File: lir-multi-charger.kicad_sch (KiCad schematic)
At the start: 46 parts, among them J1 USB_C_Receptacle_USB2.0_16P, J2 Conn_01x02_Pin, J3 Conn_01x02_Pin, J4 Conn_01x02_Pin, J5 Conn_01x02_Pin, J6 Conn_01x02_Pin, J7 Conn_01x02_Socket, J8 Conn_01x02_Socket, J9 Conn_01x02_Socket, U1 CN3130, U2 CN3130, U3 CN3130

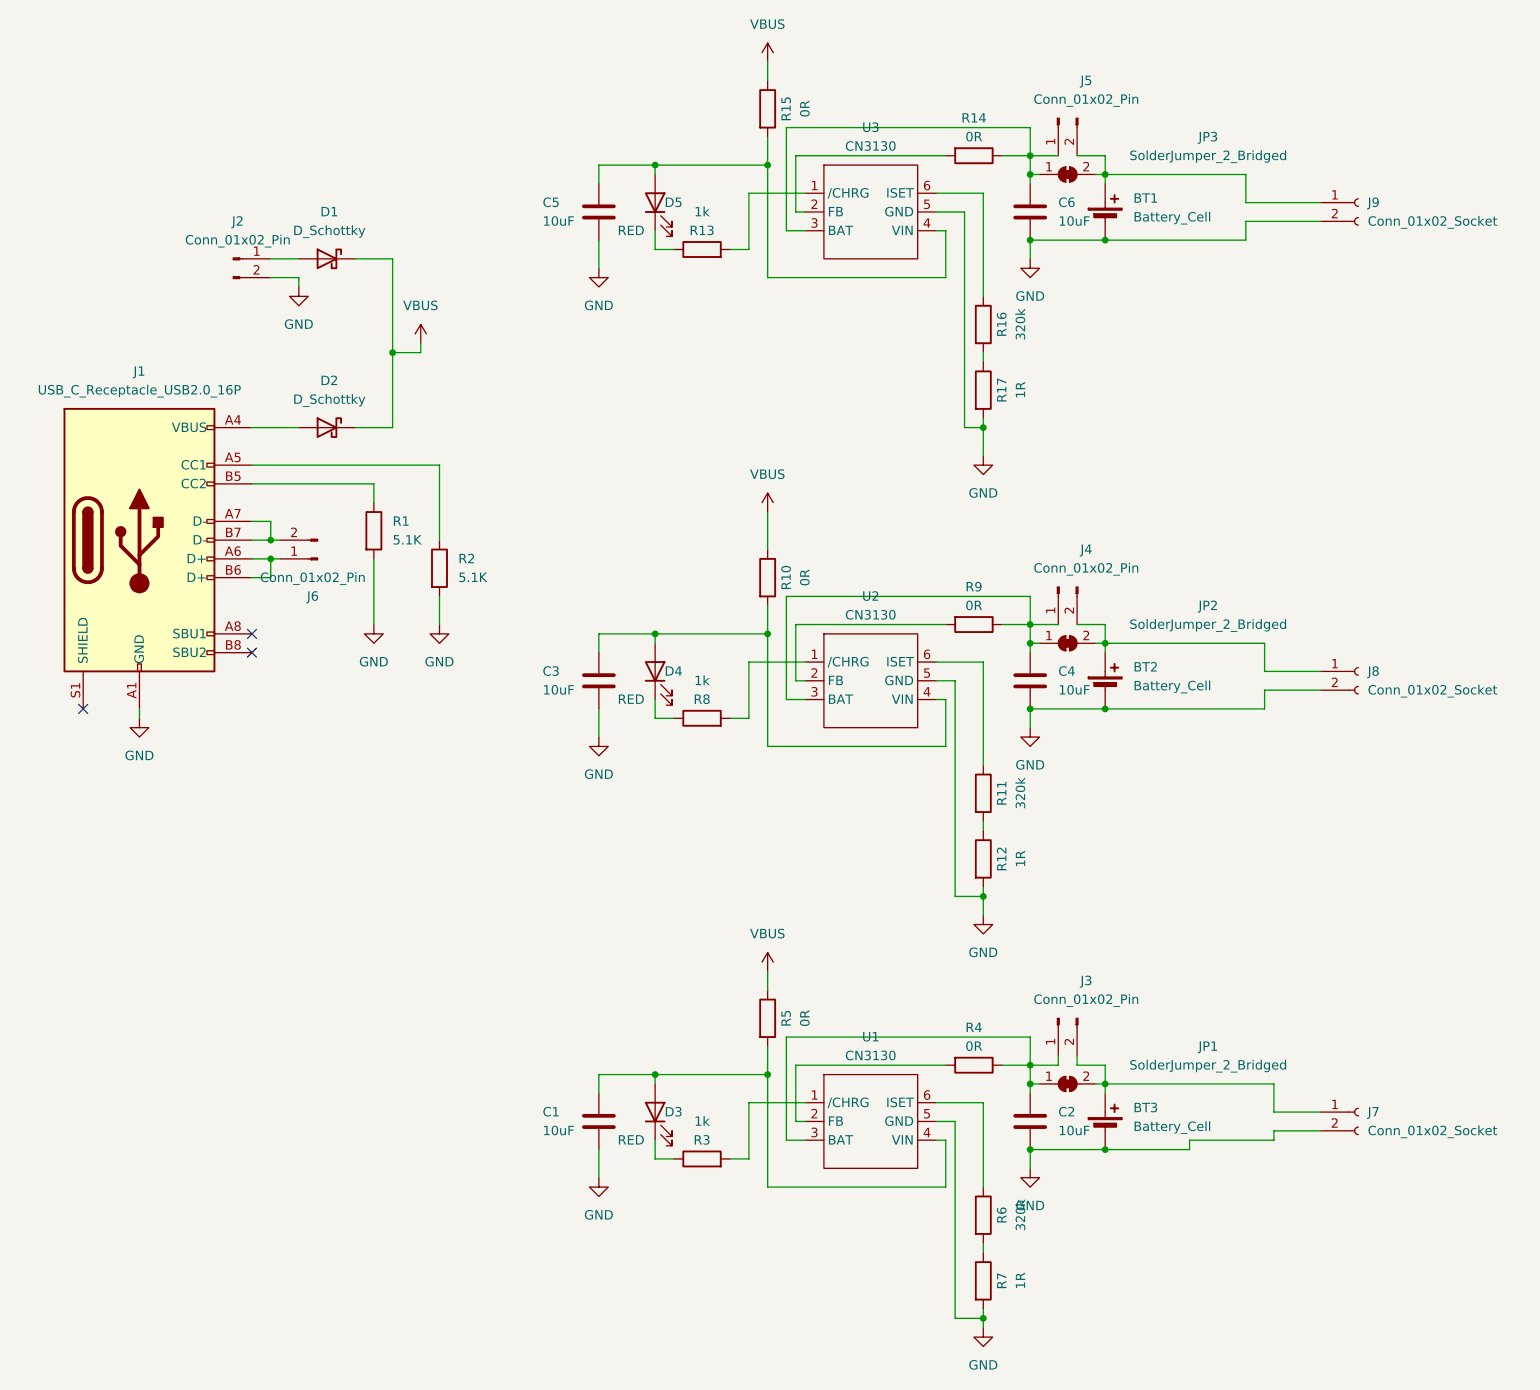
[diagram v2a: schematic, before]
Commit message: Update PCB design: modify resistor values and add labels for better readability
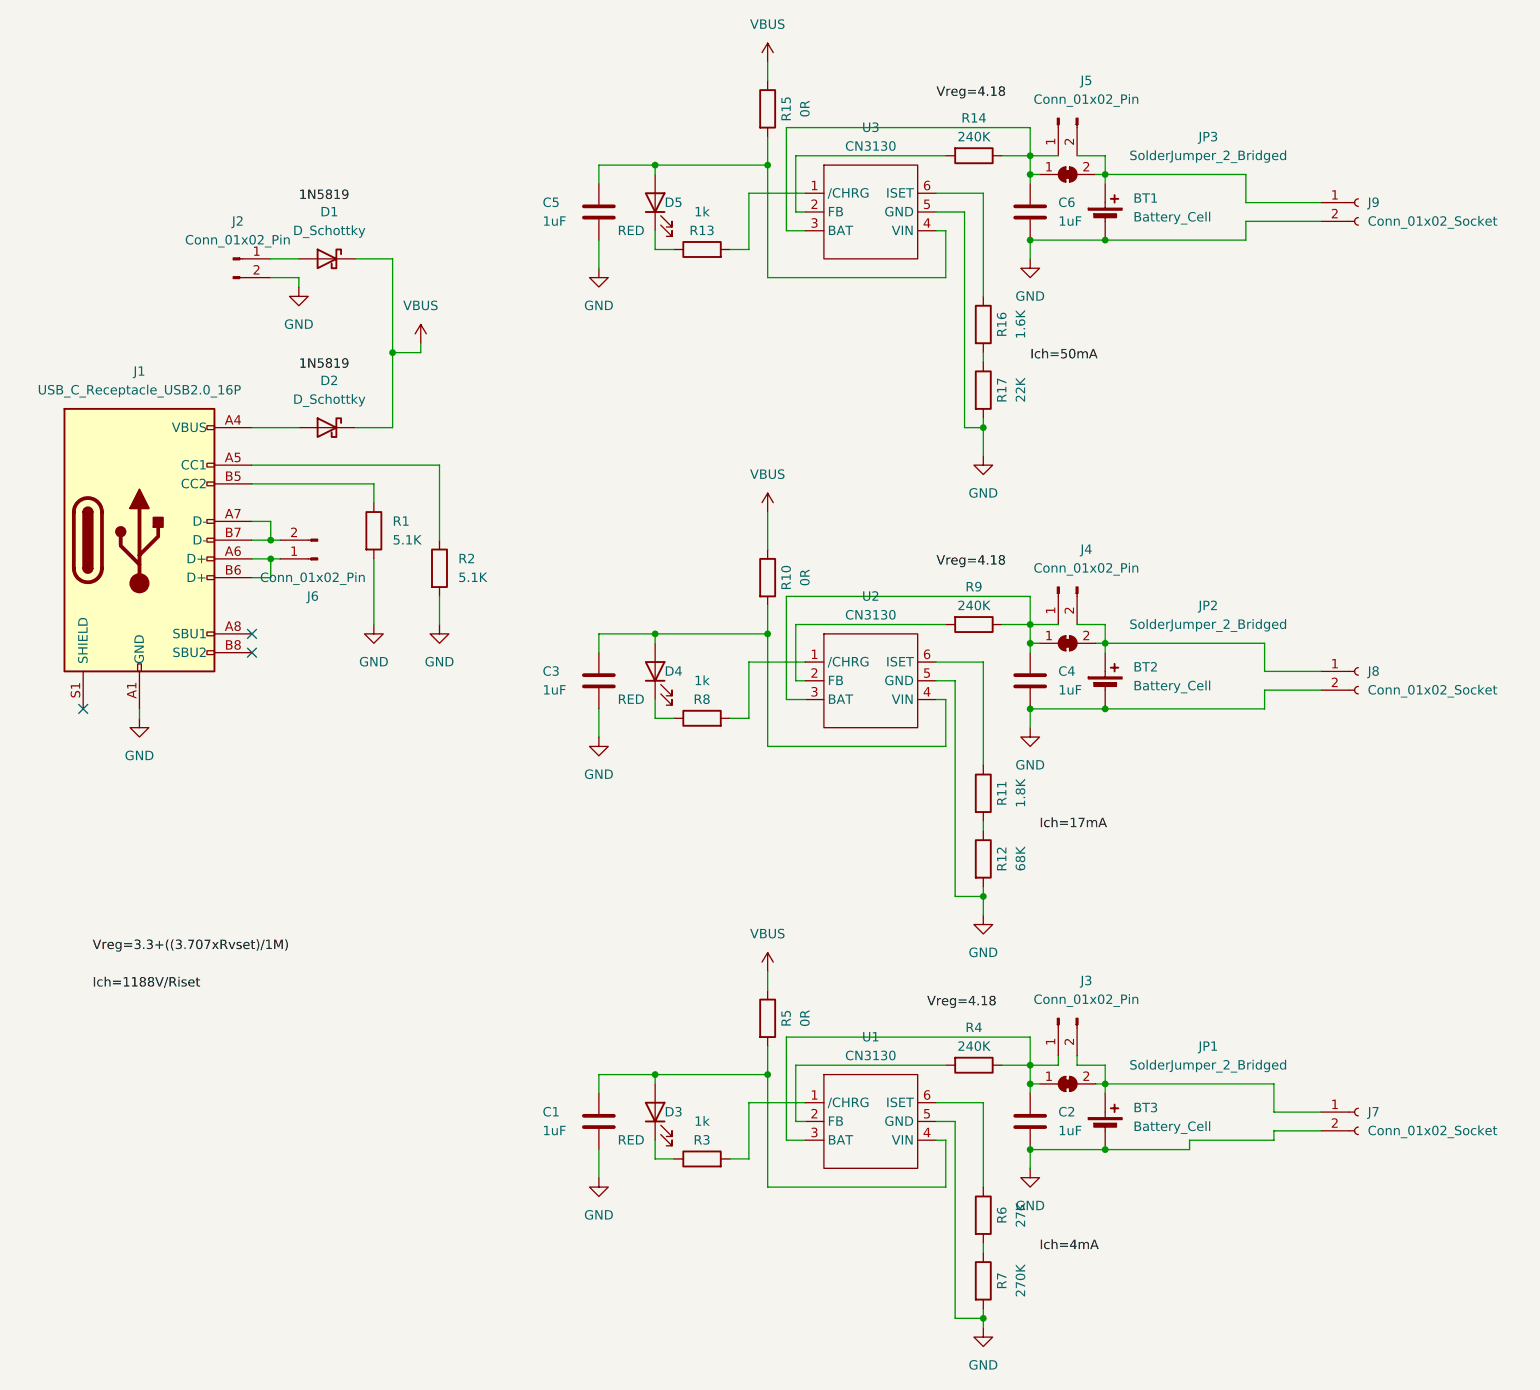
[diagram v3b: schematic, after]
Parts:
- C1, C2, C3, C4, C5, C6: value 10uF -> 1uF
- R11: value 320k -> 1.8K
- R12: value 1R -> 68K
- R14, R4, R9: value 0R -> 240K
- R16: value 320k -> 1.6K
- R17: value 1R -> 22K
- R6: value 320k -> 27K
- R7: value 1R -> 270K
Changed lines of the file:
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@@
     (stroke (width 0) (type default))
+  )
+  (label "Ich=17mA" (at 154.94 123.19 0) (fields_autoplaced)
+    (effects (font (size 1.27 1.27)) (justify left bottom))
+  )
+  (label "Vreg=4.18" (at 140.97 24.13 0) (fields_autoplaced)
+    (effects (font (size 1.27 1.27)) (justify left bottom))
+  )
+  (label "1N5819" (at 54.61 38.1 0) (fields_autoplaced)
+    (effects (font (size 1.27 1.27)) (justify left bottom))
+  )
+  (label "Vreg=4.18" (at 139.7 147.32 0) (fields_autoplaced)
+    (effects (font (size 1.27 1.27)) (justify left bottom))
+  )
+  (label "1N5819" (at 54.61 60.96 0) (fields_autoplaced)
+    (effects (font (size 1.27 1.27)) (justify left bottom))
+  )
+  (label "Ich=1188V{slash}Riset" (at 26.67 144.78 0) (fields_autoplaced)
+    (effects (font (size 1.27 1.27)) (justify left bottom))
+  )
+  (label "Vreg=4.18" (at 140.97 87.63 0) (fields_autoplaced)
+    (effects (font (size 1.27 1.27)) (justify left bottom))
+  )
+  (label "Ich=50mA" (at 153.67 59.69 0) (fields_autoplaced)
+    (effects (font (size 1.27 1.27)) (justify left bottom))
+  )
+  (label "Vreg=3.3+((3.707xRvset){slash}1M)" (at 26.67 139.7 0) (fields_autoplaced)
+    (effects (font (size 1.27 1.27)) (justify left bottom))
+  )
+  (label "Ich=4mA" (at 154.94 180.34 0) (fields_autoplaced)
+    (effects (font (size 1.27 1.27)) (justify left bottom))
   )
   (symbol (lib_id "power:GND") (at 73.66 95.25 0) (unit 1)
@@
       (effects (font (size 1.27 1.27)))
     )
-    (property "Value" "320k" (at 152.4 118.11 90)
+    (property "Value" "1.8K" (at 152.4 118.11 90)
       (effects (font (size 1.27 1.27)))
     )
@@
       (effects (font (size 1.27 1.27)))
     )
-    (property "Value" "320k" (at 152.4 175.26 90)
+    (property "Value" "27K" (at 152.4 175.26 90)
       (effects (font (size 1.27 1.27)))
     )
@@
       (effects (font (size 1.27 1.27)) (justify left))
     )
-    (property "Value" "10uF" (at 157.48 40.6399 0)
+    (property "Value" "1uF" (at 157.48 40.6399 0)
       (effects (font (size 1.27 1.27)) (justify left))
     )
@@
       (effects (font (size 1.27 1.27)))
     )
-    (property "Value" "0R" (at 146.05 29.21 90)
+    (property "Value" "240K" (at 146.05 29.21 90)
       (effects (font (size 1.27 1.27)))
     )
@@
       (effects (font (size 1.27 1.27)))
     )
-    (property "Value" "1R" (at 152.4 127 90)
+    (property "Value" "68K" (at 152.4 127 90)
       (effects (font (size 1.27 1.27)))
     )
@@
       (effects (font (size 1.27 1.27)) (justify left))
     )
-    (property "Value" "10uF" (at 157.48 163.8299 0)
+    (property "Value" "1uF" (at 157.48 163.8299 0)
       (effects (font (size 1.27 1.27)) (justify left))
     )
@@
       (effects (font (size 1.27 1.27)) (justify left))
     )
-    (property "Value" "10uF" (at 157.48 104.1399 0)
+    (property "Value" "1uF" (at 157.48 104.1399 0)
       (effects (font (size 1.27 1.27)) (justify left))
     )
@@
       (effects (font (size 1.27 1.27)) (justify left))
     )
-    (property "Value" "10uF" (at 87.63 163.83 0)
+    (property "Value" "1uF" (at 87.63 163.83 0)
       (effects (font (size 1.27 1.27)) (justify left))
     )
@@
       (effects (font (size 1.27 1.27)) (justify left))
     )
-    (property "Value" "10uF" (at 87.63 40.64 0)
+    (property "Value" "1uF" (at 87.63 40.64 0)
       (effects (font (size 1.27 1.27)) (justify left))
     )
@@
       (effects (font (size 1.27 1.27)))
     )
-    (property "Value" "1R" (at 152.4 63.5 90)
+    (property "Value" "22K" (at 152.4 63.5 90)
       (effects (font (size 1.27 1.27)))
     )
@@
       (effects (font (size 1.27 1.27)))
     )
-    (property "Value" "0R" (at 146.05 152.4 90)
+    (property "Value" "240K" (at 146.05 152.4 90)
       (effects (font (size 1.27 1.27)))
     )
@@
       (effects (font (size 1.27 1.27)))
     )
-    (property "Value" "0R" (at 146.05 92.71 90)
+    (property "Value" "240K" (at 146.05 92.71 90)
       (effects (font (size 1.27 1.27)))
     )
@@
       (effects (font (size 1.27 1.27)))
     )
-    (property "Value" "320k" (at 152.4 54.61 90)
+    (property "Value" "1.6K" (at 152.4 54.61 90)
       (effects (font (size 1.27 1.27)))
     )
@@
       (effects (font (size 1.27 1.27)) (justify left))
     )
-    (property "Value" "10uF" (at 87.63 104.14 0)
+    (property "Value" "1uF" (at 87.63 104.14 0)
       (effects (font (size 1.27 1.27)) (justify left))
     )
@@
       (effects (font (size 1.27 1.27)))
     )
-    (property "Value" "1R" (at 152.4 184.15 90)
-      (effects (font (size 1.27 1.27)))
-    )
+    (property "Value" "270K" (at 152.4 184.15 90)
+      (effects (font (size 1.27 1.27)))
+    )
